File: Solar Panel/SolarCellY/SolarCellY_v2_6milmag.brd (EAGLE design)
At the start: 100 x 82 mm, 23 parts

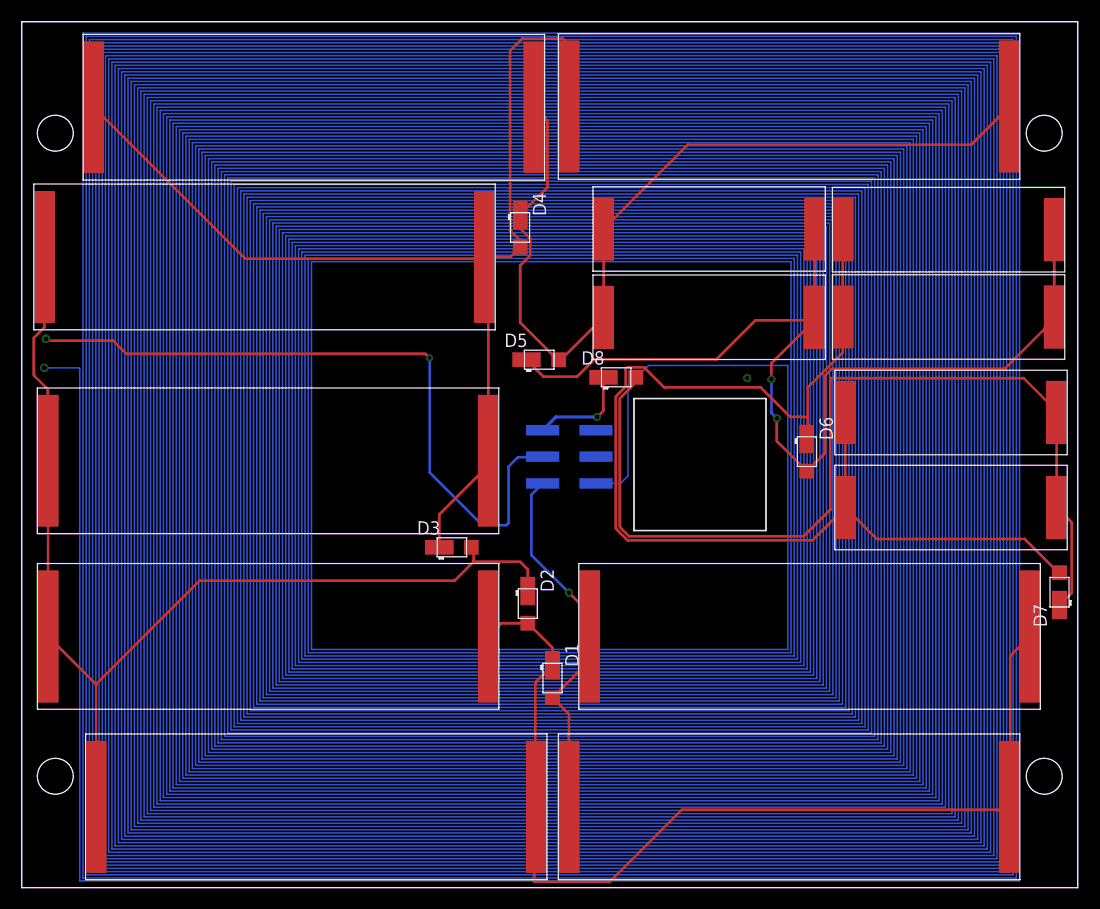
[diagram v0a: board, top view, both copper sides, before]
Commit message: Finalized Y and created gerbers
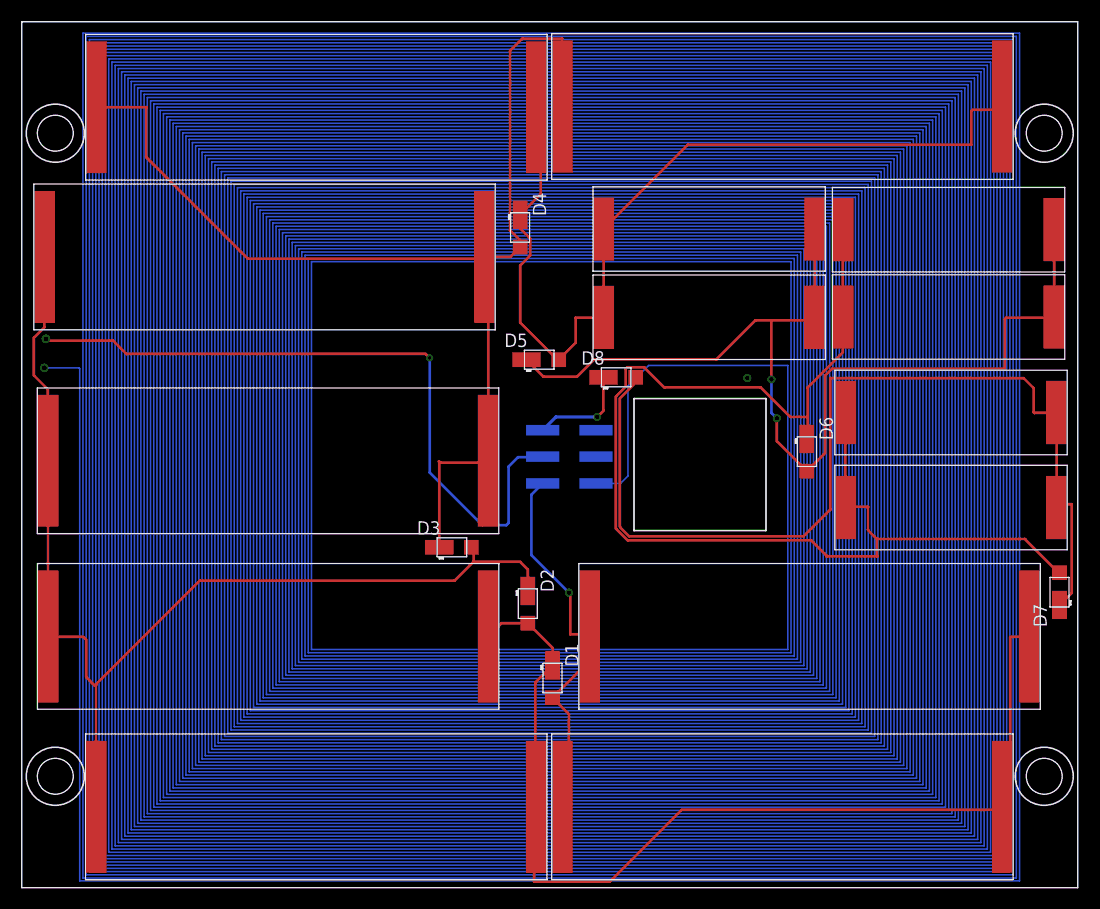
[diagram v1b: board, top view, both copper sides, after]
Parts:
- moved 24 0.64 mm to (50.2, 67.1)
- moved 11 0.63 mm to (50.2, 0.76)
- moved 23 0.24 mm to (6.05, 67.0)
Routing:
- net N$4: track 85.4 -> 91.4 mm
- net N$5: track 107.5 -> 113.0 mm
- net N$8: track 111.3 -> 116.8 mm
- net GND: track 35.4 -> 38.8 mm
- net N$10: track 90.9 -> 93.5 mm
- net N$3: track 104.4 -> 106.7 mm
- net N$6: track 98.4 -> 99.6 mm
- net N$2: track 95.4 -> 96.3 mm

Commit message: redid some spacing
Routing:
- net N$10: track 93.5 -> 92.6 mm
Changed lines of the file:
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@@
 <contactref element="U$6" pad="P$2"/>
 <contactref element="D8" pad="POS"/>
-<wire x1="58.135" y1="48.333" x2="58.135" y2="47.848" width="0.254" layer="1"/>
-<wire x1="58.135" y1="47.848" x2="56.642" y2="46.355" width="0.254" layer="1"/>
-<wire x1="56.642" y1="46.355" x2="56.642" y2="34.163" width="0.254" layer="1"/>
-<wire x1="56.642" y1="34.163" x2="57.531" y2="33.274" width="0.254" layer="1"/>
-<wire x1="57.531" y1="33.274" x2="74.041" y2="33.274" width="0.254" layer="1"/>
-<wire x1="74.041" y1="33.274" x2="76.581" y2="35.814" width="0.254" layer="1"/>
+<wire x1="58.135" y1="48.333" x2="58.135" y2="47.34" width="0.254" layer="1"/>
+<wire x1="58.135" y1="47.34" x2="57.531" y2="46.736" width="0.254" layer="1"/>
+<wire x1="57.531" y1="46.736" x2="57.531" y2="33.401" width="0.254" layer="1"/>
+<wire x1="57.531" y1="33.401" x2="74.168" y2="33.401" width="0.254" layer="1"/>
+<wire x1="74.168" y1="33.401" x2="76.581" y2="35.814" width="0.254" layer="1"/>
 <wire x1="76.581" y1="35.814" x2="76.581" y2="48.26" width="0.254" layer="1"/>
 <wire x1="76.581" y1="48.26" x2="94.869" y2="48.26" width="0.254" layer="1"/>
